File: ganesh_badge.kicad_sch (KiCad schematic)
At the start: 11 parts, among them J1 Conn_01x03_Male, J2 USB_B_Micro, SW1 SW_Push, U1 ATtiny9-TS

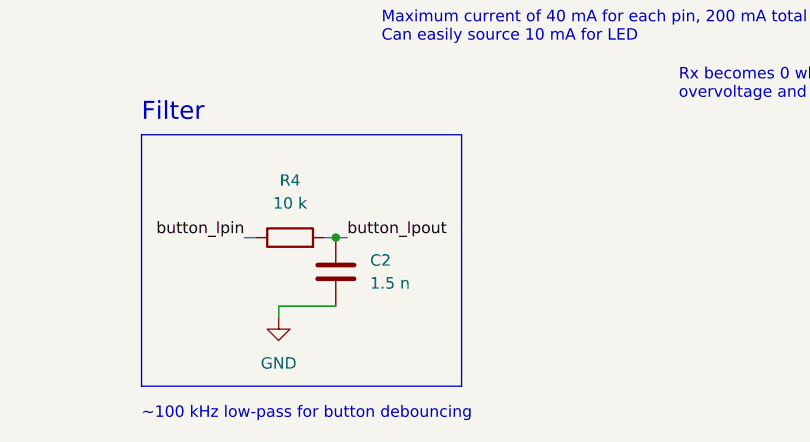
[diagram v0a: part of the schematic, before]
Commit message: simple text fixes
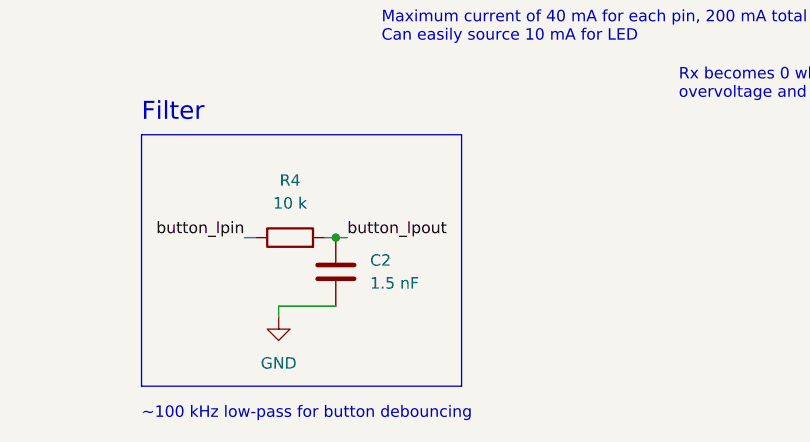
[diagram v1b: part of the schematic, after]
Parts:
- C2: value 1.5 n -> 1.5 nF
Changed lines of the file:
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@@
       (effects (font (size 1.27 1.27)) (justify left))
     )
-    (property "Value" "1.5 n" (id 1) (at 102.87 97.7899 0)
+    (property "Value" "1.5 nF" (id 1) (at 102.87 97.7899 0)
       (effects (font (size 1.27 1.27)) (justify left))
     )
@@
     )
     (path "/3897e2d8-c0f0-4e04-a843-047251b96ca8"
-      (reference "C2") (unit 1) (value "1.5 n") (footprint "Capacitor_SMD:C_0603_1608Metric")
+      (reference "C2") (unit 1) (value "1.5 nF") (footprint "Capacitor_SMD:C_0603_1608Metric")
     )
     (path "/b4c155af-8b5f-4e43-827d-fa39b2417b0c"

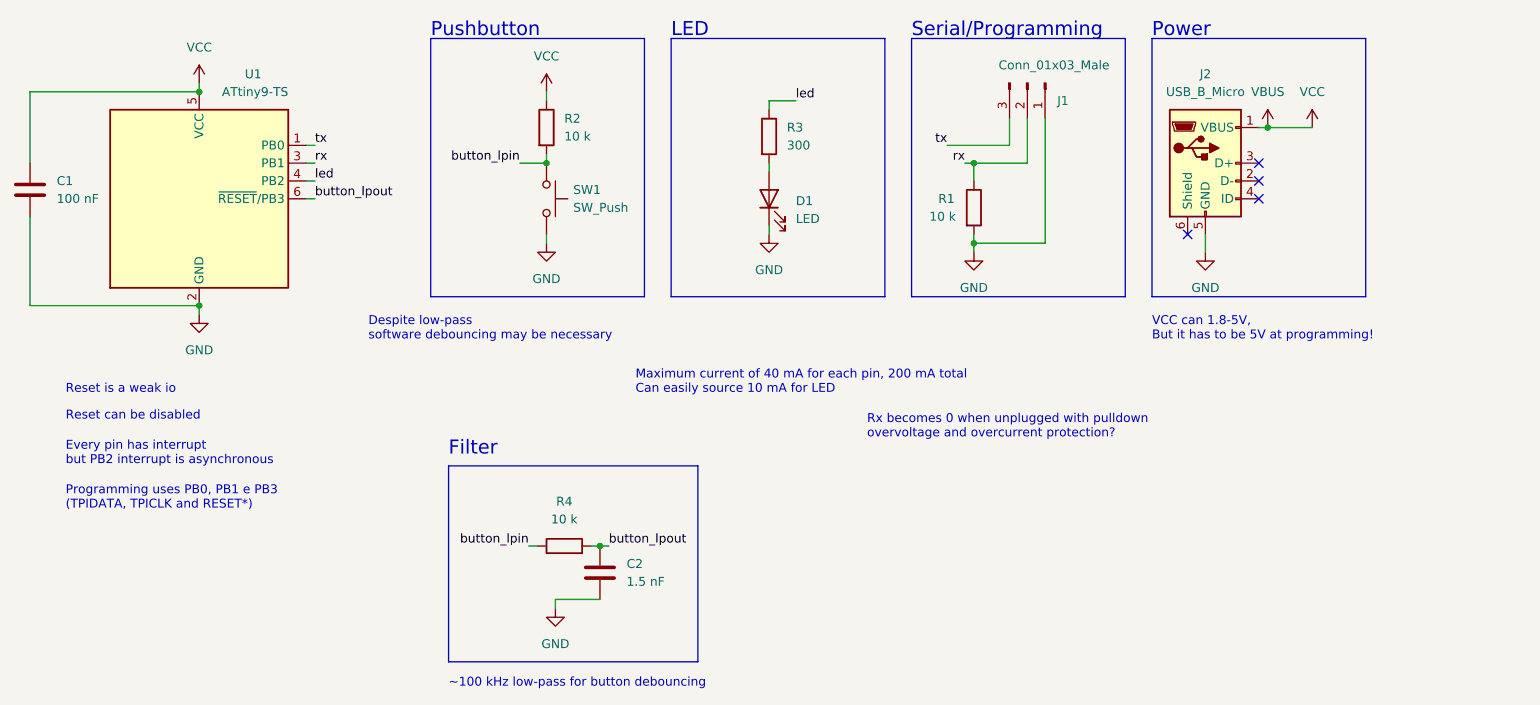
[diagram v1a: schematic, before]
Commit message: changes pic_version to main version and discards attiny
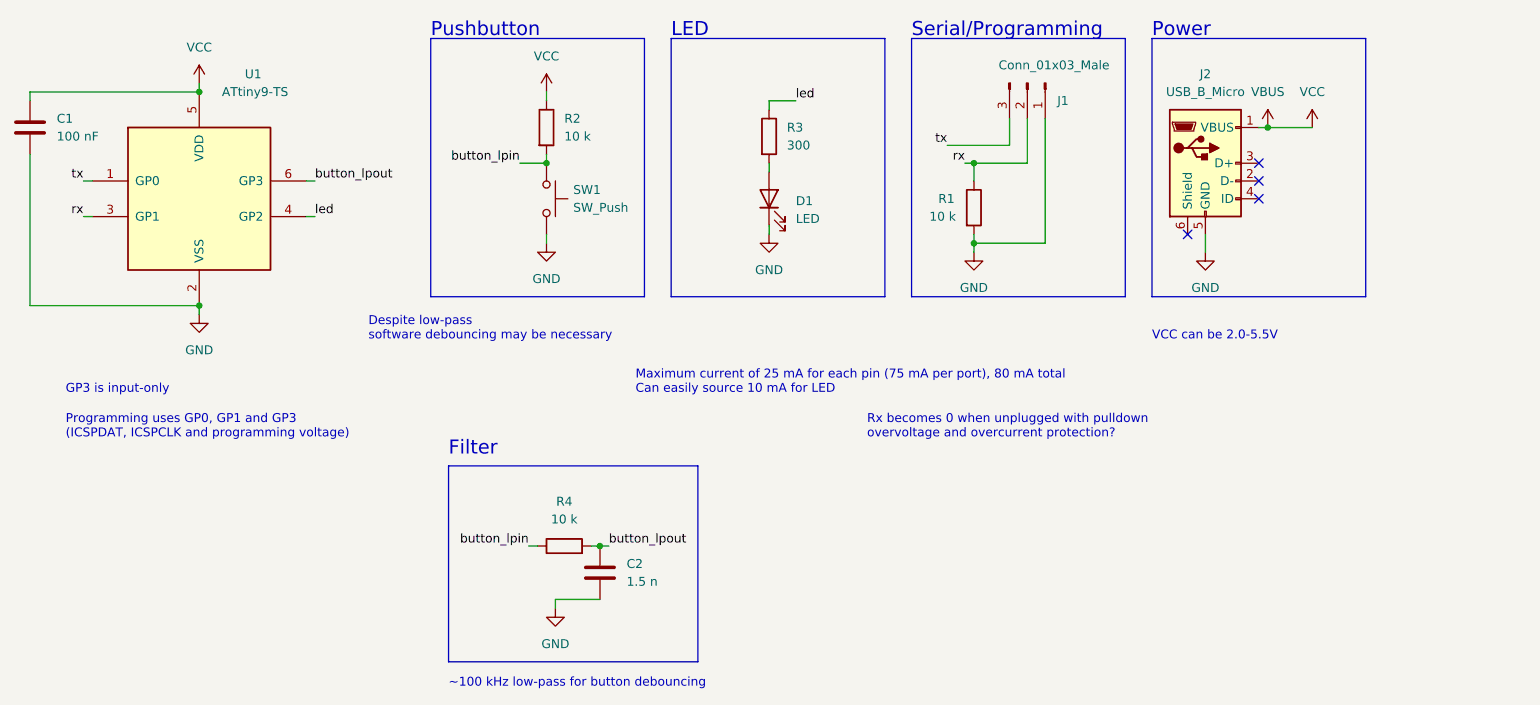
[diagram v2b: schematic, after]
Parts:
- C2: value 1.5 nF -> 1.5 n
- U1: symbol MCU_Microchip_ATtiny:ATtiny9-TS -> MCU_Microchip_PIC10:PIC10F202-IOT
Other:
- note added: "GP3 is input-only"
- note added: "Maximum current of 25 mA for each pin (75 mA per port), 80 mA total Can easily source 10 mA for LED"
- note added: "Programming uses GP0, GP1 and GP3 (ICSPDAT, ICSPCLK and programming voltage)"
- note added: "VCC can be 2.0-5.5V"
- note removed: "Every pin has interrupt but PB2 interrupt is asynchronous"
- note removed: "Maximum current of 40 mA for each pin, 200 mA total Can easily source 10 mA for LED"
- note removed: "Programming uses PB0, PB1 e PB3 (TPIDATA, TPICLK and RESET*)"
- note removed: "Reset can be disabled"
- note removed: "Reset is a weak io"
- note removed: "VCC can 1.8-5V, But it has to be 5V at programming!"
- moved on the sheet: C1, U1
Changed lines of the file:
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@@
     (stroke (width 0) (type default) (color 0 0 0 0))
   )
-  (wire (pts (xy 17.78 27.94) (xy 17.78 38.1))
+  (wire (pts (xy 17.78 27.94) (xy 17.78 29.21))
     (stroke (width 0) (type default) (color 0 0 0 0))
   )
@@
     (stroke (width 0) (type default) (color 0 0 0 0))
   )
-  (wire (pts (xy 57.15 35.56) (xy 58.42 35.56))
+  (wire (pts (xy 26.67 40.64) (xy 25.4 40.64))
     (stroke (width 0) (type default) (color 0 0 0 0))
   )
@@
     (stroke (width 0) (type default) (color 0 0 0 0))
   )
-  (wire (pts (xy 57.15 43.18) (xy 58.42 43.18))
+  (wire (pts (xy 57.15 40.64) (xy 58.42 40.64))
     (stroke (width 0) (type default) (color 0 0 0 0))
   )
@@
     (stroke (width 0) (type default) (color 0 0 0 0))
   )
-  (wire (pts (xy 17.78 45.72) (xy 17.78 58.42))
-    (stroke (width 0) (type default) (color 0 0 0 0))
-  )
-  (wire (pts (xy 57.15 40.64) (xy 58.42 40.64))
+  (wire (pts (xy 17.78 36.83) (xy 17.78 58.42))
+    (stroke (width 0) (type default) (color 0 0 0 0))
+  )
+  (wire (pts (xy 57.15 45.72) (xy 58.42 45.72))
     (stroke (width 0) (type default) (color 0 0 0 0))
   )
@@
     (stroke (width 0) (type default) (color 0 0 0 0))
   )
-  (wire (pts (xy 57.15 38.1) (xy 58.42 38.1))
+  (wire (pts (xy 26.67 45.72) (xy 25.4 45.72))
     (stroke (width 0) (type default) (color 0 0 0 0))
   )
@@
     (effects (font (size 1.27 1.27)) (justify left bottom))
   )
-  (text "Maximum current of 40 mA for each pin, 200 mA total\nCan easily source 10 mA for LED"
+  (text "Maximum current of 25 mA for each pin (75 mA per port), 80 mA total\nCan easily source 10 mA for LED"
     (at 104.14 71.12 0)
     (effects (font (size 1.27 1.27)) (justify left bottom))
@@
     (effects (font (size 1.27 1.27)) (justify left bottom))
   )
-  (text "Programming uses PB0, PB1 e PB3\n(TPIDATA, TPICLK and RESET*)"
-    (at 22.86 87.63 0)
-    (effects (font (size 1.27 1.27)) (justify left bottom))
-  )
-  (text "Reset can be disabled" (at 22.86 74.93 0)
+  (text "Programming uses GP0, GP1 and GP3\n(ICSPDAT, ICSPCLK and programming voltage)"
+    (at 22.86 77.47 0)
     (effects (font (size 1.27 1.27)) (justify left bottom))
   )
@@
     (effects (font (size 2 2)) (justify left bottom))
   )
-  (text "VCC can 1.8-5V,\nBut it has to be 5V at programming!"
-    (at 177.8 63.5 0)
+  (text "VCC can be 2.0-5.5V" (at 177.8 63.5 0)
     (effects (font (size 1.27 1.27)) (justify left bottom))
   )
@@
     (effects (font (size 2 2)) (justify left bottom))
   )
-  (text "Every pin has interrupt\nbut PB2 interrupt is asynchronous"
-    (at 22.86 81.28 0)
-    (effects (font (size 1.27 1.27)) (justify left bottom))
-  )
   (text "LED" (at 109.22 20.32 0)
     (effects (font (size 2 2)) (justify left bottom))
   )
-  (text "Reset is a weak io" (at 22.86 71.12 0)
+  (text "GP3 is input-only" (at 22.86 71.12 0)
     (effects (font (size 1.27 1.27)) (justify left bottom))
   )
@@
     (effects (font (size 1.27 1.27)) (justify right bottom))
   )
-  (label "button_lpout" (at 58.42 43.18 0)
-    (effects (font (size 1.27 1.27)) (justify left bottom))
-  )
-  (label "tx" (at 58.42 35.56 0)
-    (effects (font (size 1.27 1.27)) (justify left bottom))
-  )
-  (label "rx" (at 58.42 38.1 0)
-    (effects (font (size 1.27 1.27)) (justify left bottom))
+  (label "button_lpout" (at 58.42 40.64 0)
+    (effects (font (size 1.27 1.27)) (justify left bottom))
+  )
+  (label "tx" (at 25.4 40.64 180)
+    (effects (font (size 1.27 1.27)) (justify right bottom))
+  )
+  (label "rx" (at 25.4 45.72 180)
+    (effects (font (size 1.27 1.27)) (justify right bottom))
   )
   (label "led" (at 127 29.21 0)
@@
     (effects (font (size 1.27 1.27)) (justify right bottom))
   )
-  (label "led" (at 58.42 40.64 0)
+  (label "led" (at 58.42 45.72 0)
     (effects (font (size 1.27 1.27)) (justify left bottom))
   )
@@
     (pin "1")
   )
-  (symbol (lib_id "Device:C") (at 17.78 41.91 0) (unit 1)
-    (in_bom yes) (on_board yes) (fields_autoplaced)
-    (property "Reference" "C1" (id 0) (at 21.59 40.6399 0)
-      (effects (font (size 1.27 1.27)) (justify left))
-    )
-    (property "Value" "100 nF" (id 1) (at 21.59 43.1799 0)
-      (effects (font (size 1.27 1.27)) (justify left))
-    )
-    (property "Footprint" "Capacitor_SMD:C_0603_1608Metric" (id 2) (at 18.7452 45.72 0)
-      (effects (font (size 1.27 1.27)) hide)
-    )
-    (property "Datasheet" "~" (id 3) (at 17.78 41.91 0)
+  (symbol (lib_id "Device:C") (at 17.78 33.02 0) (unit 1)
+    (in_bom yes) (on_board yes) (fields_autoplaced)
+    (property "Reference" "C1" (id 0) (at 21.59 31.7499 0)
+      (effects (font (size 1.27 1.27)) (justify left))
+    )
+    (property "Value" "100 nF" (id 1) (at 21.59 34.2899 0)
+      (effects (font (size 1.27 1.27)) (justify left))
+    )
+    (property "Footprint" "Capacitor_SMD:C_0603_1608Metric" (id 2) (at 18.7452 36.83 0)
+      (effects (font (size 1.27 1.27)) hide)
+    )
+    (property "Datasheet" "~" (id 3) (at 17.78 33.02 0)
       (effects (font (size 1.27 1.27)) hide)
     )
@@
       (effects (font (size 1.27 1.27)) (justify left))
     )
-    (property "Value" "1.5 nF" (id 1) (at 102.87 97.7899 0)
+    (property "Value" "1.5 n" (id 1) (at 102.87 97.7899 0)
       (effects (font (size 1.27 1.27)) (justify left))
     )
@@
     (pin "2")
   )
-  (symbol (lib_id "MCU_Microchip_ATtiny:ATtiny9-TS") (at 41.91 43.18 0) (unit 1)
+  (symbol (lib_id "MCU_Microchip_PIC10:PIC10F202-IOT") (at 41.91 43.18 0) (unit 1)
     (in_bom yes) (on_board yes)
     (property "Reference" "U1" (id 0) (at 50.8 25.4 0)
@@
       (effects (font (size 1.27 1.27)) (justify right))
     )
-    (property "Footprint" "Custom_Footprints:SOT-23-6_narrow" (id 2) (at 41.91 43.18 0)
-      (effects (font (size 1.27 1.27) italic) hide)
-    )
-    (property "Datasheet" "http://ww1.microchip.com/downloads/en/DeviceDoc/Atmel-8127-AVR-8-bit-Microcontroller-ATtiny4-ATtiny5-ATtiny9-ATtiny10_Datasheet.pdf" (id 3) (at 41.91 43.18 0)
+    (property "Footprint" "Custom_Footprints:SOT-23-6_narrow" (id 2) (at 43.18 26.67 0)
+      (effects (font (size 1.27 1.27) italic) (justify left) hide)
+    )
+    (property "Datasheet" "http://ww1.microchip.com/downloads/en/DeviceDoc/41239D.pdf" (id 3) (at 41.91 43.18 0)
       (effects (font (size 1.27 1.27)) hide)
     )
@@
     )
     (path "/3897e2d8-c0f0-4e04-a843-047251b96ca8"
-      (reference "C2") (unit 1) (value "1.5 nF") (footprint "Capacitor_SMD:C_0603_1608Metric")
+      (reference "C2") (unit 1) (value "1.5 n") (footprint "Capacitor_SMD:C_0603_1608Metric")
     )
     (path "/b4c155af-8b5f-4e43-827d-fa39b2417b0c"

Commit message: changed header to be more compatible with pickit3
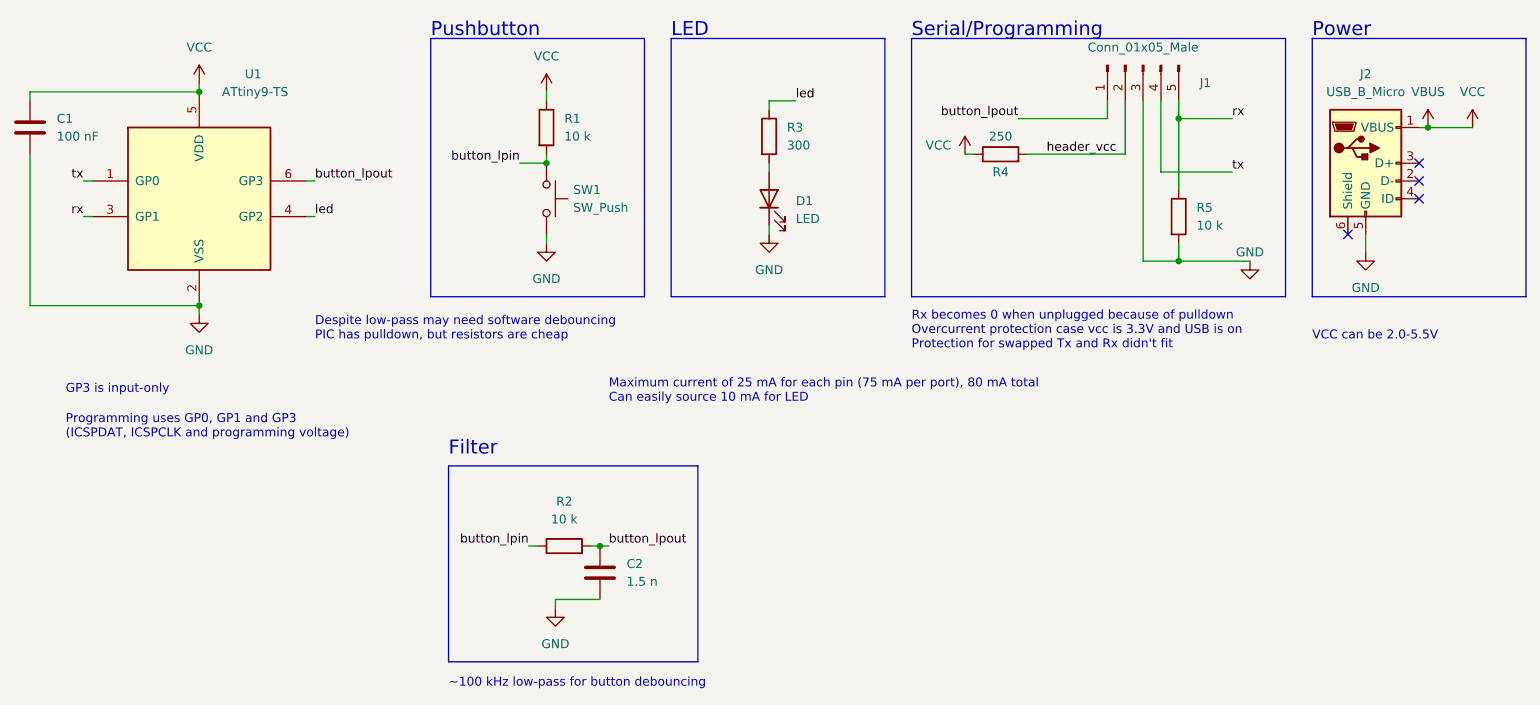
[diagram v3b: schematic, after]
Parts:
- added R4: 250, Resistor_SMD:R_0603_1608Metric, symbol Device:R
- J1: value Conn_01x03_Male -> Conn_01x05_Male; footprint Connector_PinHeader_2.00mm:PinHeader_1x03_P2.00mm_Vertical -> Connector_PinHeader_2.54mm:PinHeader_1x05_P2.54mm_Vertical; symbol Connector:Conn_01x03_Male -> Connector:Conn_01x05_Male; now in the parts list
- renumbered R2 to R1, R4 to R2, R1 to R5
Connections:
- net GND: now also J1.3 (Pin_3); no longer J1.1 (Pin_1)
- net VBUS: now also R4.1
- net button_lpout: now also J1.1 (Pin_1)
- net rx: now also J1.5 (Pin_5); no longer J1.2 (Pin_2)
- net tx: now also J1.4 (Pin_4); no longer J1.3 (Pin_3)
- new net header_vcc: J1.2 (Pin_2), R4.2
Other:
- note added: "Despite low-pass may need software debouncing PIC has pulldown, but resistors are cheap"
- note added: "Rx becomes 0 when unplugged because of pulldown Overcurrent protection case vcc is 3.3V and USB is on Protection for swapped Tx and Rx didn't fit"
- note removed: "Despite low-pass software debouncing may be necessary"
- note removed: "Rx becomes 0 when unplugged with pulldown overvoltage and overcurrent protection?"
- moved on the sheet: J2, R5
